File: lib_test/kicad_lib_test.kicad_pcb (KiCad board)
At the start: 2 copper layers, 130 x 80 mm, 245 parts

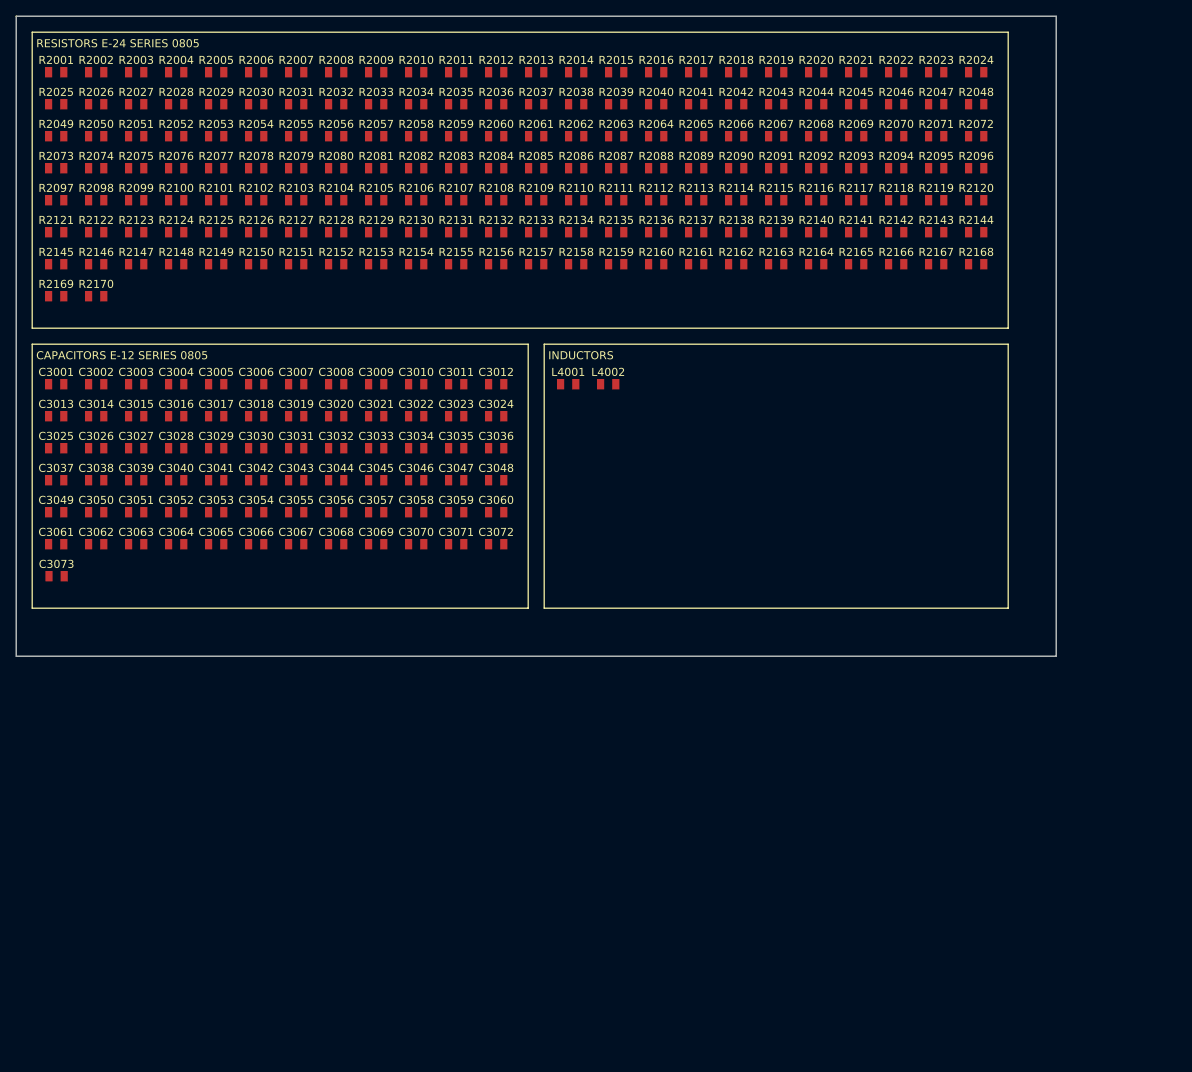
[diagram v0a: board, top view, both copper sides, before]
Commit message: add capacitor 4u7 50V 1206
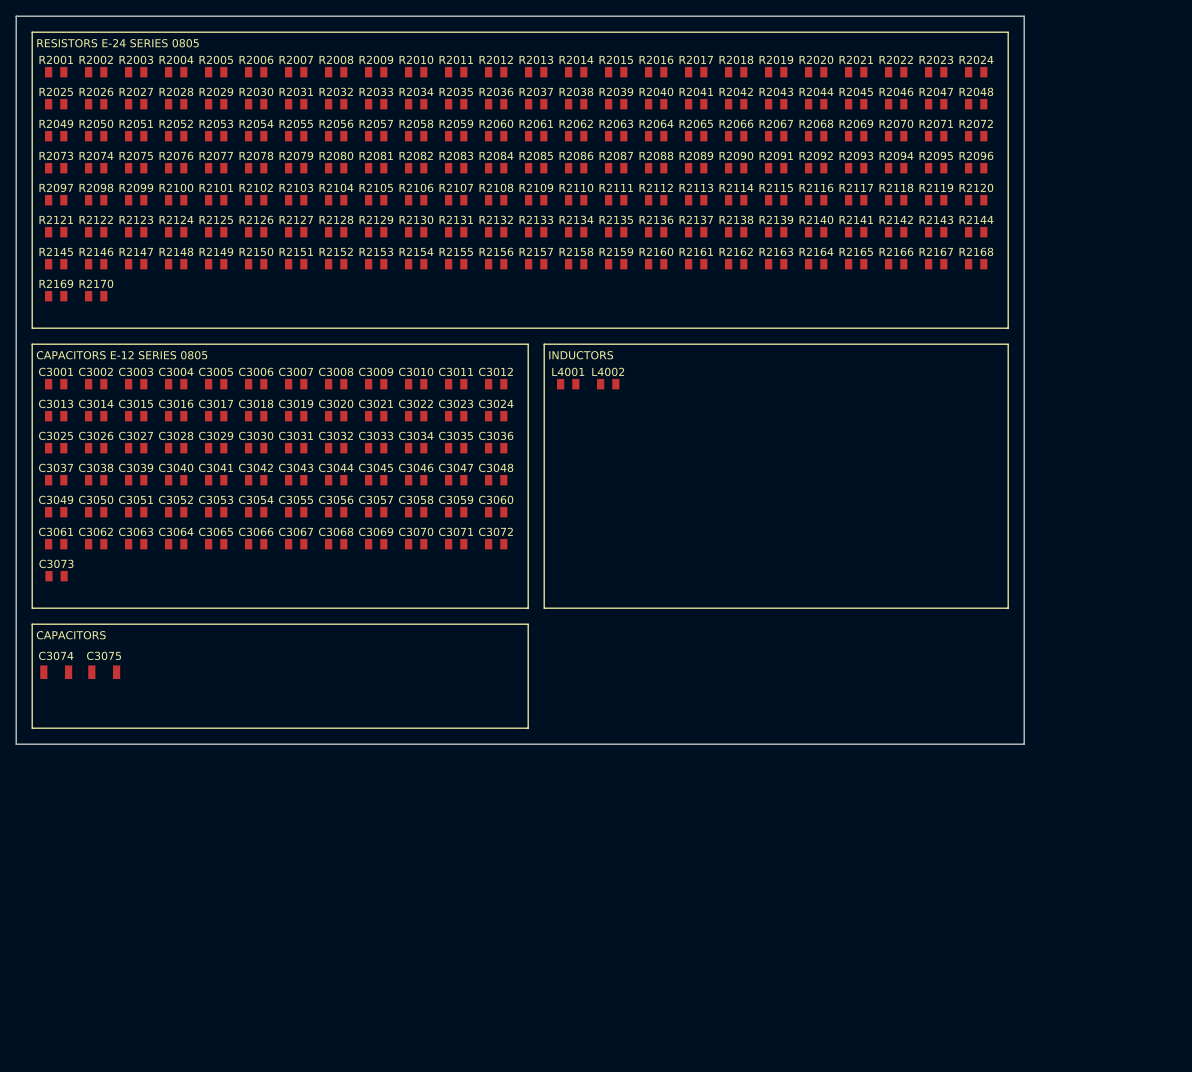
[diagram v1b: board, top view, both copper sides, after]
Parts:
- added C3074: 4u7, lily_footprints:cap_1206, F.Cu at (25.0, 102.0)
- added C3075: dnp, lily_footprints:cap_1206_dnp, F.Cu at (31.0, 102.0)
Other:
- board size 130 x 80 mm -> 126 x 91 mm
- board text added: "CAPACITORS"

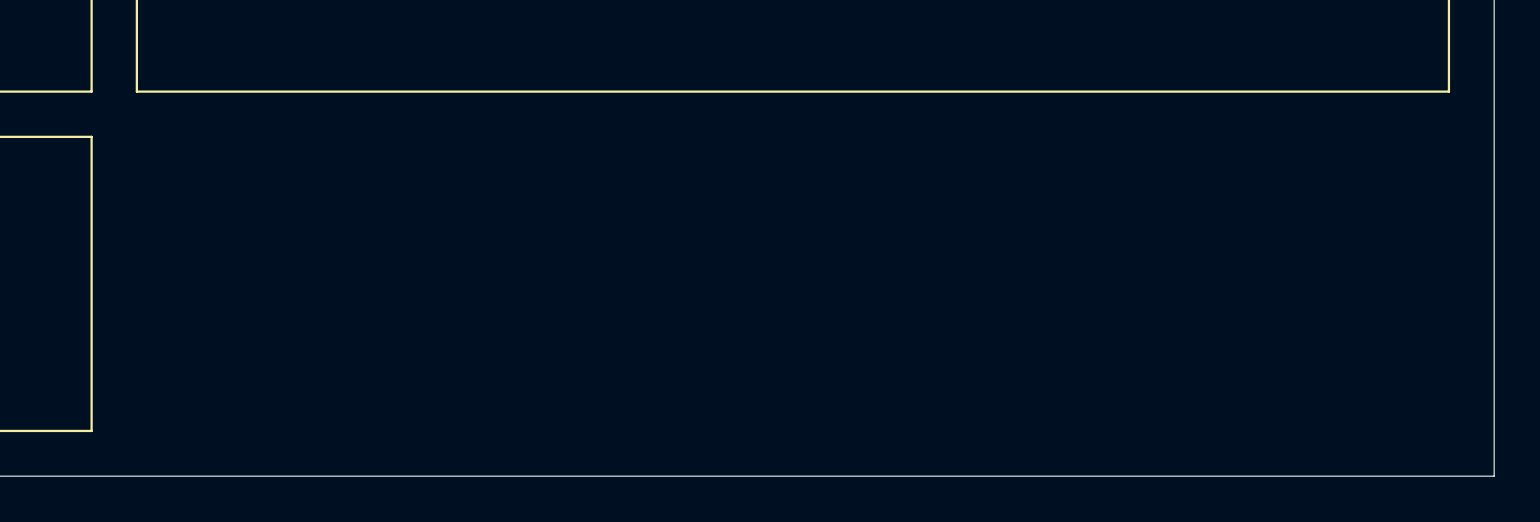
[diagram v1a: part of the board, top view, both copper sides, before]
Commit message: add diode tvs uni 2 channel 12V
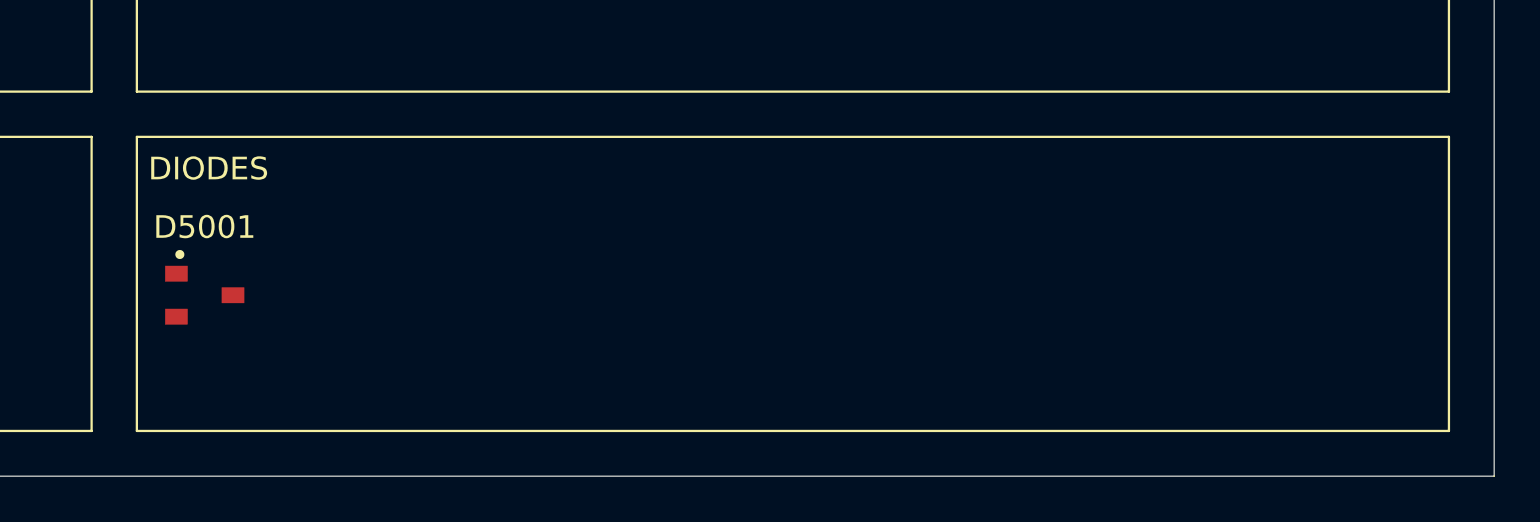
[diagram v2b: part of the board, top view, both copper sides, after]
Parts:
- added D5001: dio_tvs_uni_2_channel, lily_footprints:sot23, F.Cu at (89.0, 103.0)
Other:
- board text added: "DIODES"

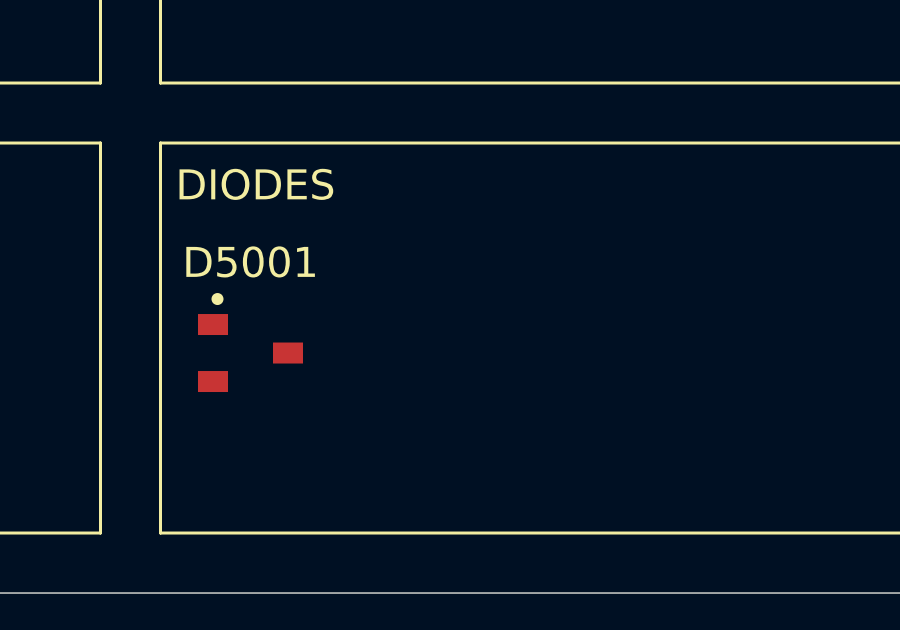
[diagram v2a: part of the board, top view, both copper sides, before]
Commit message: add diode SS14
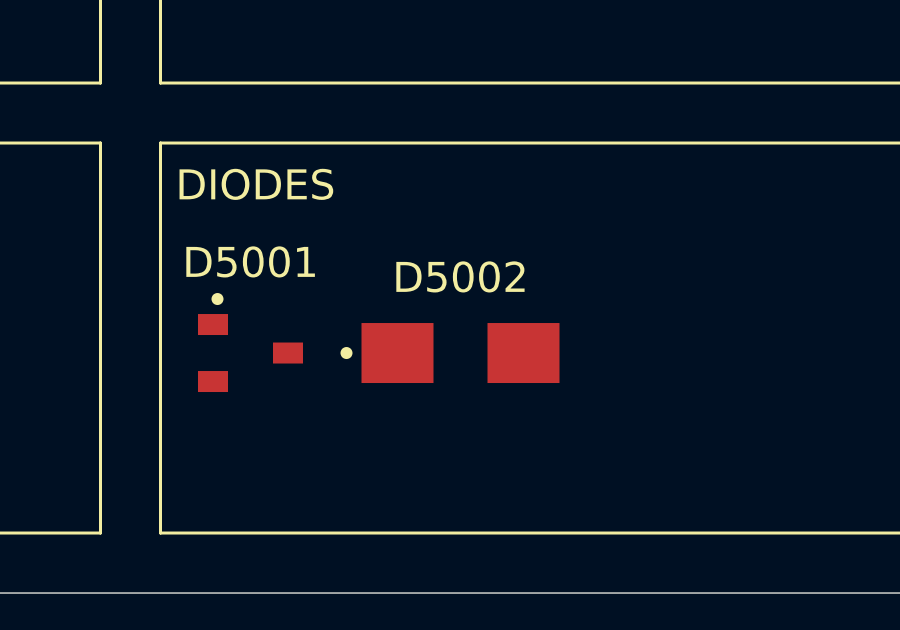
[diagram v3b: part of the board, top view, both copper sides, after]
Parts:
- added D5002: SS14, lily_footprints:dio_do214ac_sma, F.Cu at (96.0, 103.0)
- D5001: value dio_tvs_uni_2_channel -> 15V

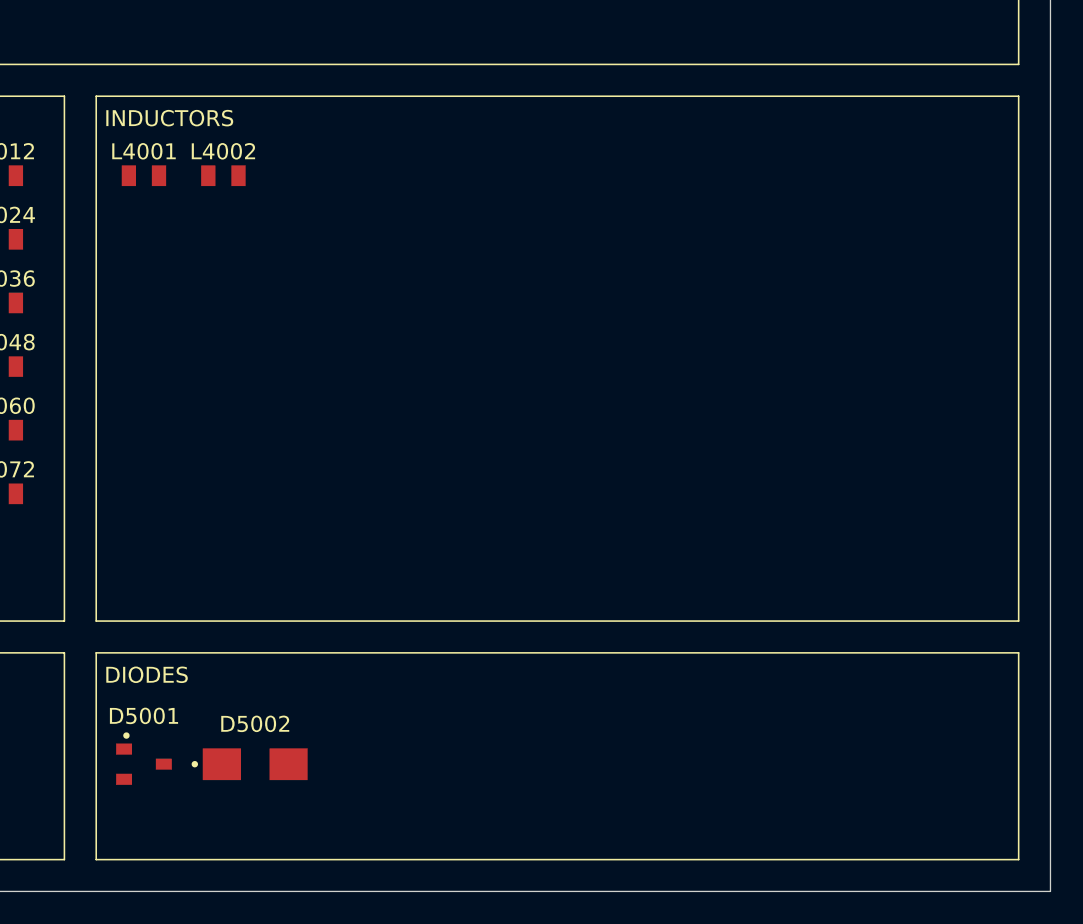
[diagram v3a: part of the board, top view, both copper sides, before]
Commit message: add MOSFET AO3400A
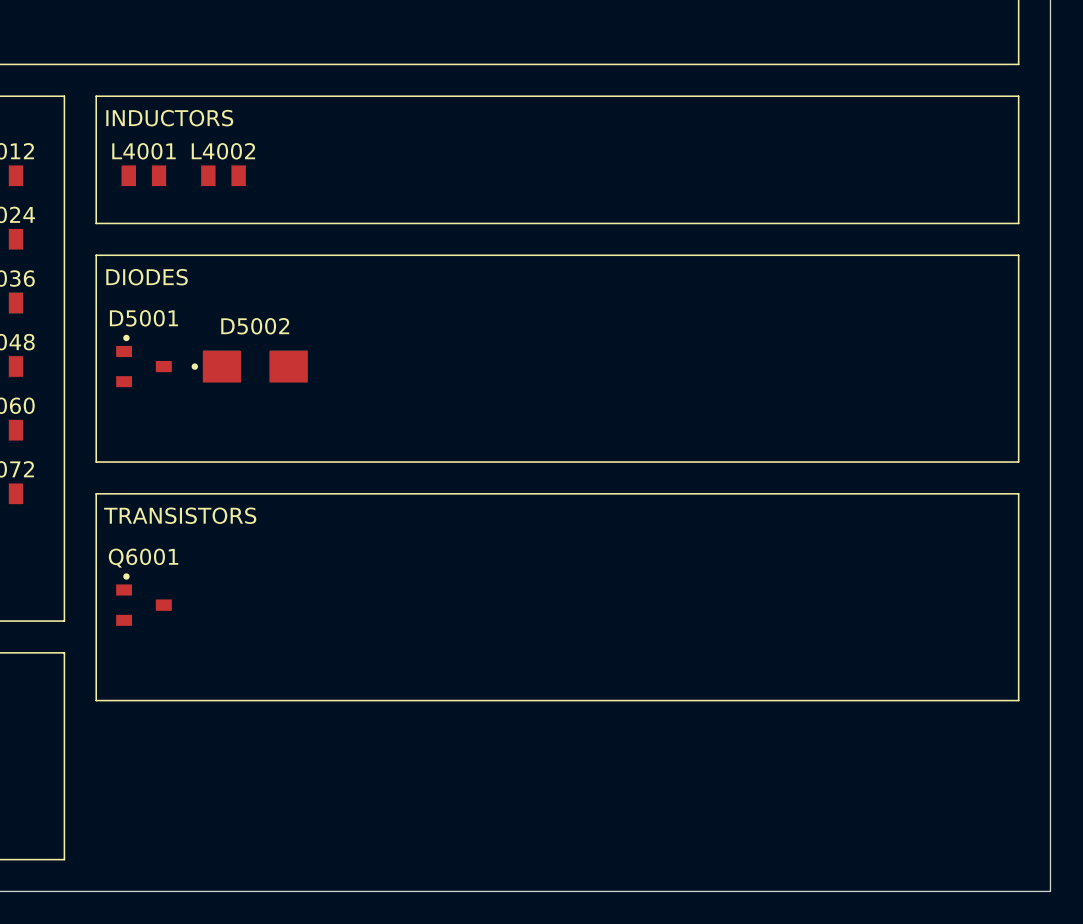
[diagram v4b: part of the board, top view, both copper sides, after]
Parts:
- added Q6001: AO3400A, lily_footprints:sot23, F.Cu at (89.0, 93.0)
- moved D5001 25.0 mm to (89.0, 78.0)
- moved D5002 25.0 mm to (96.0, 78.0)
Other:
- board text added: "TRANSISTORS"

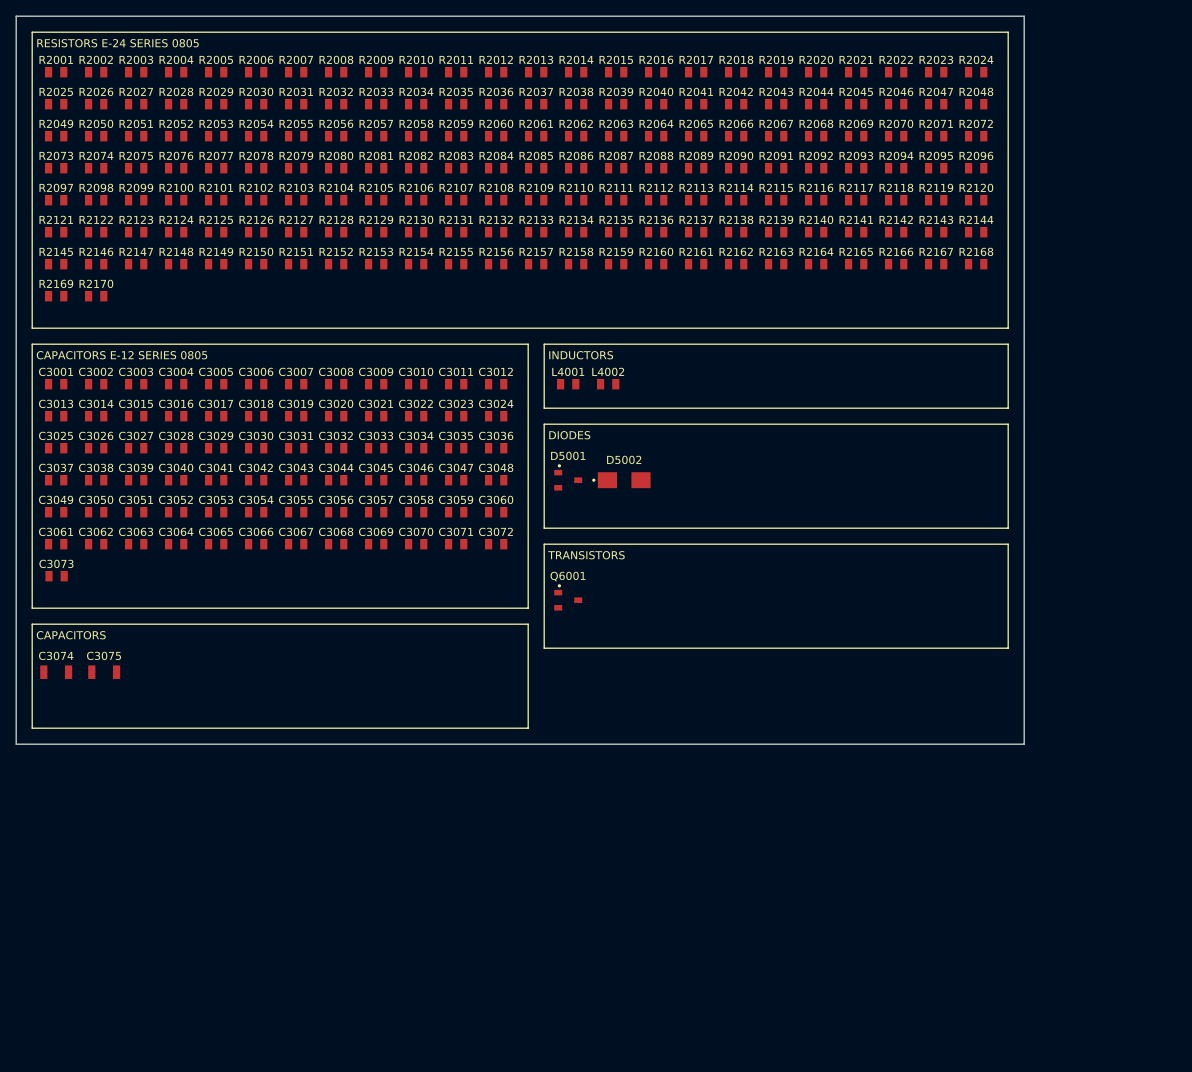
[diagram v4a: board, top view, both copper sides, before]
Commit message: add dual opamp TLV272
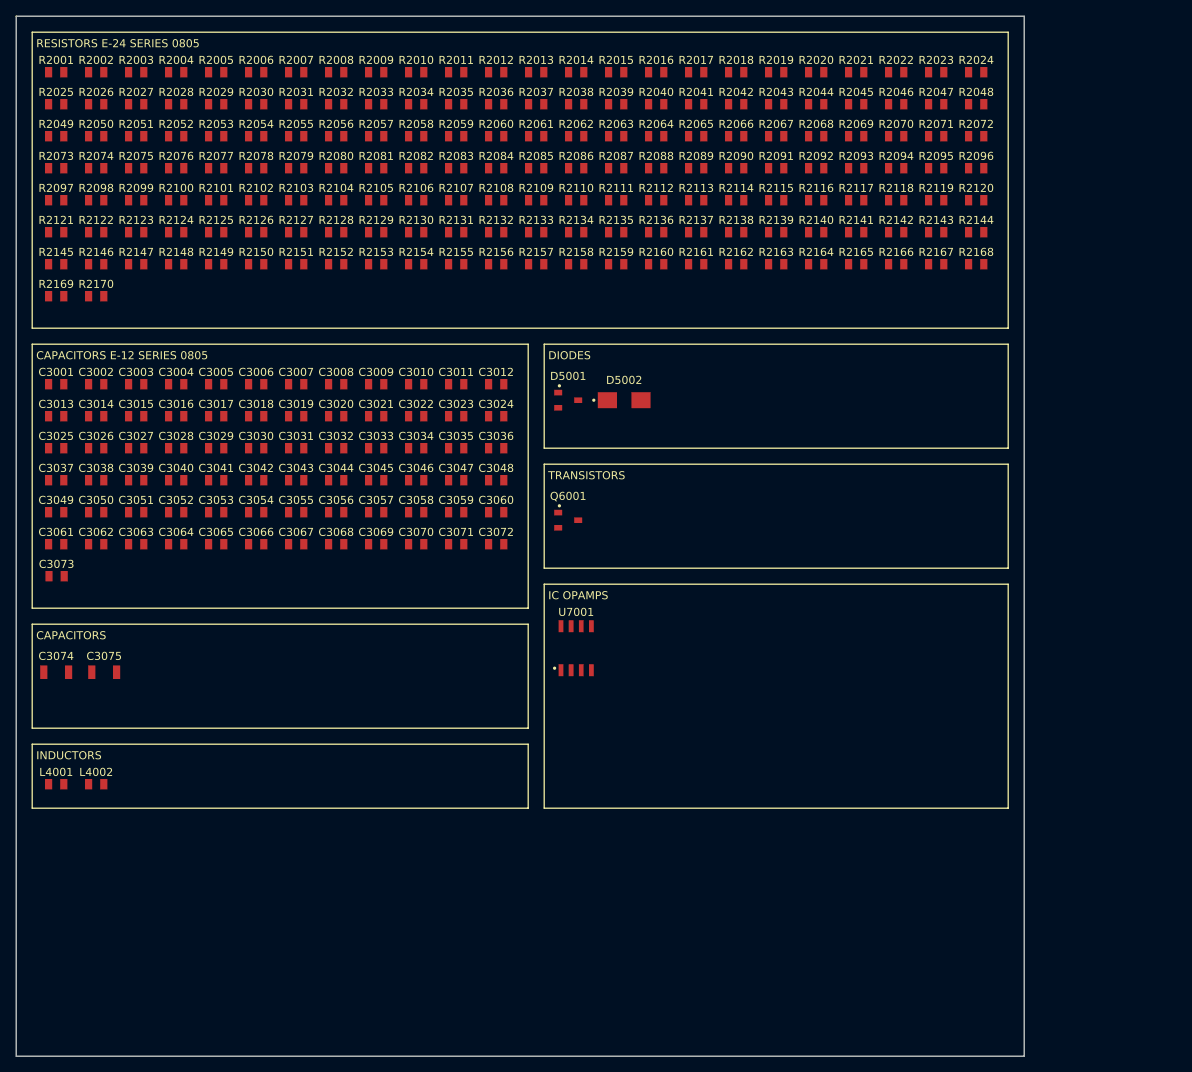
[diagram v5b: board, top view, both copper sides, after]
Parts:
- added U7001: TLV272, lily_footprints:soic8, F.Cu at (90.0, 99.0)
- moved L4001 81.2 mm to (25.0, 116.0)
- moved L4002 81.2 mm to (30.0, 116.0)
- moved D5001 10.0 mm to (89.0, 68.0)
- moved D5002 10.0 mm to (96.0, 68.0)
- moved Q6001 10.0 mm to (89.0, 83.0)
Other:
- board size 126 x 91 mm -> 126 x 130 mm
- board text added: "IC OPAMPS"

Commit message: add new parts
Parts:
- added U8001: LM335, lily_footprints:to92, F.Cu at (119.0, 66.0)
- moved D5001 76.0 mm to (25.0, 109.0)
- moved D5002 76.0 mm to (32.0, 109.0)
- moved Q6001 41.2 mm to (57.0, 109.0)
- moved L4001 37.2 mm to (57.0, 97.0)
- moved L4002 37.2 mm to (62.0, 97.0)
- moved U7001 32.0 mm to (90.0, 67.0)
- moved C3074 4.00 mm to (25.0, 98.0)
- moved C3075 4.00 mm to (31.0, 98.0)
- moved C3001 2.00 mm to (25.0, 64.0)
- moved C3002 2.00 mm to (30.0, 64.0)
- moved C3003 2.00 mm to (35.0, 64.0)
- moved C3004 2.00 mm to (40.0, 64.0)
- moved C3005 2.00 mm to (45.0, 64.0)
- moved C3006 2.00 mm to (50.0, 64.0)
- moved C3007 2.00 mm to (55.0, 64.0)
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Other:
- board size 126 x 130 mm -> 126 x 94 mm
- board text added: "IC SENSORS"
